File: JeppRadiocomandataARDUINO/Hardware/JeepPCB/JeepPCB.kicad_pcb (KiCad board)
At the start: 2 copper layers, 43 x 60 mm, 21 parts, among them J1 Radio, U1 ATmega328P-A, Y1 Crystal

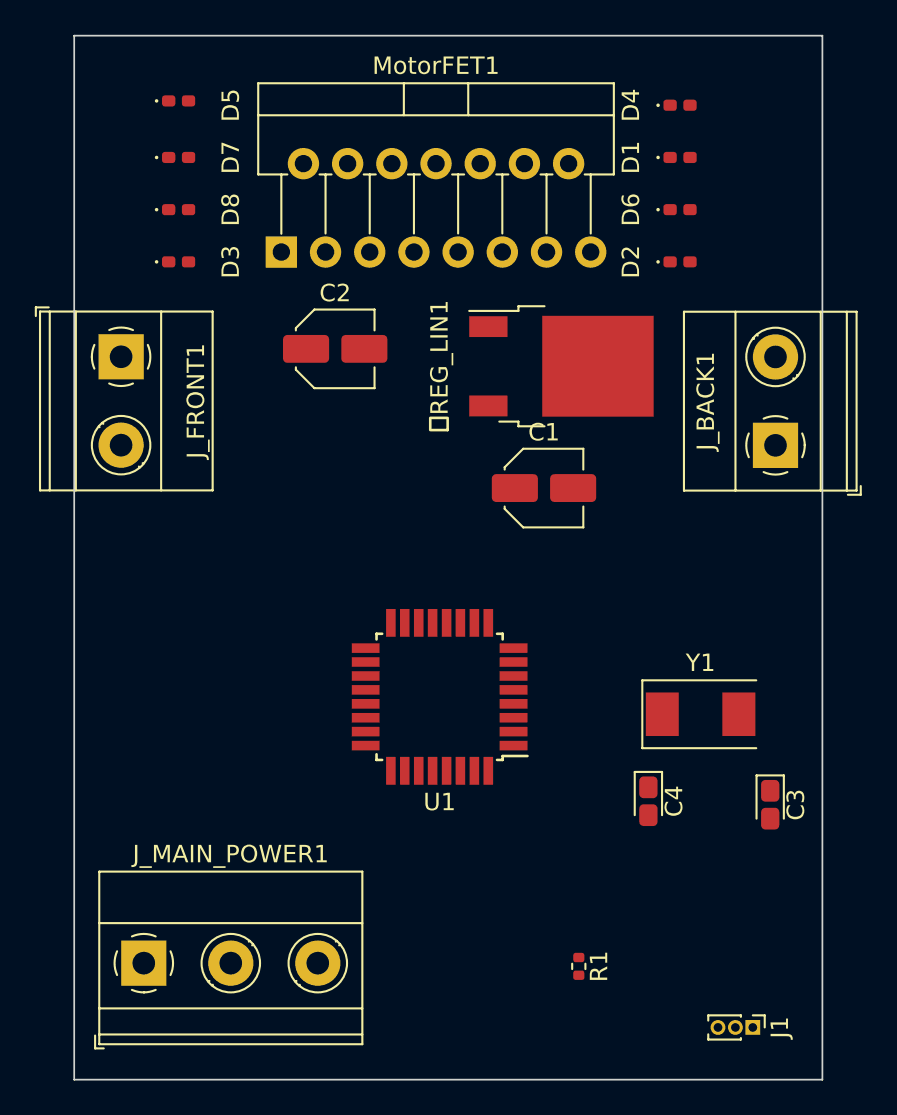
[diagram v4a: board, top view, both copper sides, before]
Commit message: Collegamento delle tracce
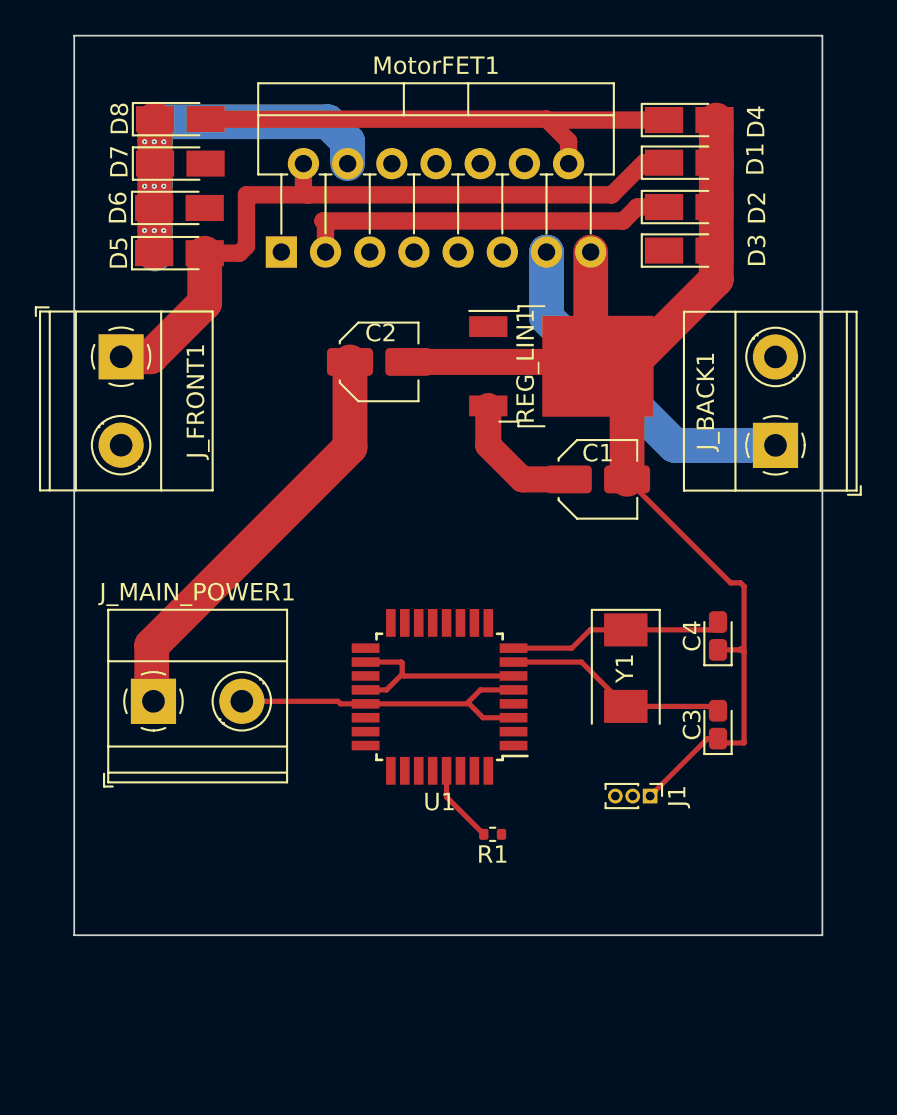
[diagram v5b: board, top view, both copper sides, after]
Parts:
- D1, D2, D3, D4, D5, D6, D7, D8: footprint Diode_SMD:D_0402_1005Metric_Pad0.77x0.64mm_HandSolder -> Diode_SMD:D_MicroMELF_Handsoldering
- J_MAIN_POWER1: value Screw_Terminal_01x03 -> Screw_Terminal_01x02; footprint TerminalBlock_Phoenix:TerminalBlock_Phoenix_MKDS-1,5-3_1x03_P5.00mm_Horizontal -> TerminalBlock_Phoenix:TerminalBlock_Phoenix_MKDS-1,5-2-5.08_1x02_P5.08mm_Horizontal
- moved D3 29.4 mm to (75.3, 52.4)
- moved D6 28.8 mm to (46.0, 49.9)
- moved C1 16.9 mm to (70.1, 65.5)
- moved J_MAIN_POWER1 15.1 mm to (44.6, 78.3)
- moved J1 14.5 mm to (73.1, 83.7)
- moved C2 11.9 mm to (57.5, 58.8)
- moved C4 10.3 mm to (77.0, 74.5), turned to 90 degrees
- moved R1 9.06 mm to (64.0, 85.9), turned to 180 degrees
- moved D5 8.75 mm to (46.0, 52.5)
- moved C3 5.49 mm to (77.0, 79.6), turned to 90 degrees
- moved D8 5.20 mm to (46.1, 44.8)
- moved Y1 5.05 mm to (71.7, 76.3), turned to -90 degrees
- moved D2 3.19 mm to (75.3, 49.9)
- moved D4 1.00 mm to (75.3, 44.9)
- moved D1 0.61 mm to (75.3, 47.3)
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- renumbered C2 to C1, C1 to C2, REG_LIN1 to REG_LIN1
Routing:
- net Earth: track 0.00 -> 88.5 mm
- net /5-12V: track 0.00 -> 52.4 mm, vias 0 -> 9
- net Net-(D1-Pad1): track 0.00 -> 41.3 mm
- net Net-(D4-Pad1): track 0.00 -> 29.4 mm
- net Net-(D2-Pad1): track 0.00 -> 21.8 mm
- net Net-(D3-Pad1): track 0.00 -> 20.9 mm
- net VCC: track 0.00 -> 19.4 mm
- net Net-(C3-Pad2): track 0.00 -> 12.9 mm
- net Net-(C4-Pad2): track 0.00 -> 12.4 mm
- net Net-(R1-Pad2): track 0.00 -> 4.54 mm
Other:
- board size 43 x 60 mm -> 43 x 51.7 mm

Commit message: Modifiche alla scheda
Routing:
- net Net-(D3-Pad1): track 20.9 -> 30.7 mm
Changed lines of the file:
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@@
   (segment (start 67.145 52.435) (end 67.145 53.345) (width 2) (layer "B.Cu") (net 6))
   (segment (start 67.145 56.195) (end 74.495 63.545) (width 2) (layer "B.Cu") (net 6))
+  (segment (start 67.145 50.605) (end 67.145 52.435) (width 1) (layer "B.Cu") (net 6))
   (segment (start 74.495 63.545) (end 80.305 63.545) (width 2) (layer "B.Cu") (net 6))
+  (segment (start 72.65 52.4) (end 70.35 50.1) (width 1) (layer "B.Cu") (net 6))
+  (segment (start 67.65 50.1) (end 67.145 50.605) (width 1) (layer "B.Cu") (net 6))
+  (segment (start 70.35 50.1) (end 67.65 50.1) (width 1) (layer "B.Cu") (net 6))
+  (segment (start 73.95 52.4) (end 72.65 52.4) (width 1) (layer "B.Cu") (net 6))
   (segment (start 68.415 46.065) (end 68.415 47.355) (width 1) (layer "F.Cu") (net 7))
   (segment (start 73.9 44.85) (end 67.2 44.85) (width 1) (layer "F.Cu") (net 7))

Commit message: Aggiornamento delle tracce
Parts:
- moved D3 6.80 mm to (75.5, 45.5)
- moved D5 4.40 mm to (46.0, 48.1)
- moved D4 1.86 mm to (75.5, 43.0)
- moved D7 1.85 mm to (46.0, 45.5)
- moved D8 1.85 mm to (46.0, 43.0)
- moved D2 0.87 mm to (75.5, 50.7)
- moved D1 0.82 mm to (75.5, 48.1)
- moved D6 0.66 mm to (46.0, 50.5)
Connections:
- MotorFET1 pad 11: INO_D5 -> INO_D6
- MotorFET1 pad 12: INO_D6 -> INO_D5
- MotorFET1 pad 5: INO_D9 -> INO_D10
- MotorFET1 pad 6: INO_D10 -> INO_D9
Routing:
- net /5-12V: track 52.4 -> 109.3 mm
- net Net-(D3-Pad1): track 30.7 -> 59.9 mm, vias 0 -> 3
- net Net-(D4-Pad1): track 29.4 -> 54.7 mm, vias 0 -> 5
- net Net-(D2-Pad1): track 21.8 -> 43.6 mm
- net Net-(D1-Pad1): track 41.3 -> 44.2 mm, vias 0 -> 4
- net Earth: track 88.5 -> 90.5 mm

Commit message: Jeep Finita
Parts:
- moved R1 2.88 mm to (61.5, 84.7), turned to 90 degrees
- renumbered REG_LIN1 to RL1
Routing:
- net VCC: track 19.4 -> 122.9 mm, vias 0 -> 6
- net INO_D7: track 0.00 -> 29.4 mm, vias 0 -> 3
- net INO_D5: track 0.00 -> 29.2 mm, vias 0 -> 3
- net INO_D9: track 0.00 -> 29.2 mm, vias 0 -> 3
- net INO_D6: track 0.00 -> 24.3 mm, vias 0 -> 3
- net INO_D10: track 0.00 -> 24.0 mm, vias 0 -> 3
- net INO_D8: track 0.00 -> 23.7 mm, vias 0 -> 3
- net Net-(D3-Pad1): track 59.9 -> 57.2 mm
- net Net-(R1-Pad2): track 4.54 -> 1.91 mm
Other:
- board size 43 x 51.7 mm -> 43 x 48.2 mm
